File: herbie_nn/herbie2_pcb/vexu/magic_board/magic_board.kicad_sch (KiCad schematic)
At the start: 87 parts, among them J1 4P4C, J2 Conn_ARM_JTAG_SWD_10, J3 USB_C_Receptacle_USB2.0_14P, J4 Conn_01x04_Socket, J5 Conn_01x05_Pin, J6 Conn_01x05_Pin, J7 Conn_01x05_Pin, Q2 MMBT3904, U11 74LVC125, U12 AMS1117-5.0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

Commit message: added level shifters for led strips
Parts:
- added C14: 22uF, Capacitor_SMD:C_1206_3216Metric, symbol Device:C
- added U3, U9: 74LVC2T45DC, Package_SO:VSSOP-8_2.3x2mm_P0.5mm, symbol Logic_LevelTranslator:74LVC2T45DC
- C1, C2: value 15pF -> 12pF
- R4, R5, R6: value 330 -> 2K
- Y2: footprint Crystal:Crystal_SMD_2012-2Pin_2.0x1.2mm_HandSoldering -> Crystal:Crystal_SMD_5032-2Pin_5.0x3.2mm
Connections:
- net +12V: now also C14.1
- net +3.3V: now also U3.1 (VCCA), U3.5 (DIR), U9.1 (VCCA), U9.5 (DIR)
- net +5V: now also U3.8 (VCCB), U9.8 (VCCB)
- net GND: now also C14.2, U3.4 (GND), U9.4 (GND)
- net LED_SIG1: now also U3.2 (1A); no longer LEDSTRIP1.2 (Pin_2)
- net LED_SIG2: now also U9.2 (1A); no longer LEDSTRIP2.2 (Pin_2)
- net LED_SIG3: now also U3.3 (2A); no longer LEDSTRIP3.2 (Pin_2)
- new net LED_SIG1_OUT: LEDSTRIP1.2 (Pin_2), U3.7 (1B)
- new net LED_SIG2_OUT: LEDSTRIP2.2 (Pin_2), U9.7 (1B)
- new net LED_SIG3_OUT: LEDSTRIP3.2 (Pin_2), U3.6 (2B)
- no-connect marks 33 -> 35
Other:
- moved on the sheet: ENC1, ENC2, ENC3, ENC4, JP1, JP2, JP3, JP4, LED1, LED2, LEDSTRIP1, LEDSTRIP2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

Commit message: updated board
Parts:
- removed JP_D+1, JP_D-1, JP_RX1, JP_TX1: Jumper, Jumper:SolderJumper-2_P1.3mm_Open_Pad1.0x1.5mm, symbol Jumper:SolderJumper_2_Bridged
- added F2: 1A, Fuse:Fuse_1206_3216Metric, symbol Device:Fuse
- added PWR2: Jumper, Jumper:SolderJumper-2_P1.3mm_Open_Pad1.0x1.5mm, symbol Jumper:SolderJumper_2_Bridged
- added TP1, TP2: TestPoint, TestPoint:TestPoint_Pad_1.0x1.0mm, symbol Connector:TestPoint
- R13: value R -> 0K
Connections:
- net +12V: now also PWR2.2 (B); no longer J1.4, LEDSTRIP1.3 (Pin_3), LEDSTRIP2.3 (Pin_3), LEDSTRIP3.3 (Pin_3)
- net +3.3V: now also J4.3 (Pin_3); no longer J4.1 (Pin_1)
- net +5V: now also LEDSTRIP1.1 (Pin_1), LEDSTRIP2.1 (Pin_1), LEDSTRIP3.1 (Pin_1), F2.1; no longer D3.1 (K)
- net GND: now also LEDSTRIP1.3 (Pin_3), LEDSTRIP2.3 (Pin_3), LEDSTRIP3.3 (Pin_3); no longer LEDSTRIP1.1 (Pin_1), LEDSTRIP2.1 (Pin_1), LEDSTRIP3.1 (Pin_1)
- net RX_BRAIN: now also U4.59 (PB30)
- net SCL: now also J4.1 (Pin_1); no longer J4.2 (Pin_2)
- net SDA: now also J4.2 (Pin_2); no longer J4.3 (Pin_3)
- net TX_BRAIN: now also U4.60 (PB31)
- net at R2.1: now also U1.7 (B)
- net at U1.6 (A): now also R1.1
- net at U4.39 (PB16): now also TP1.1
- net at U4.40 (PB17): now also TP2.1
- new net: D3.1 (K), F2.2
- new net: J1.4, PWR2.1 (A)
- no-connect marks 35 -> 33

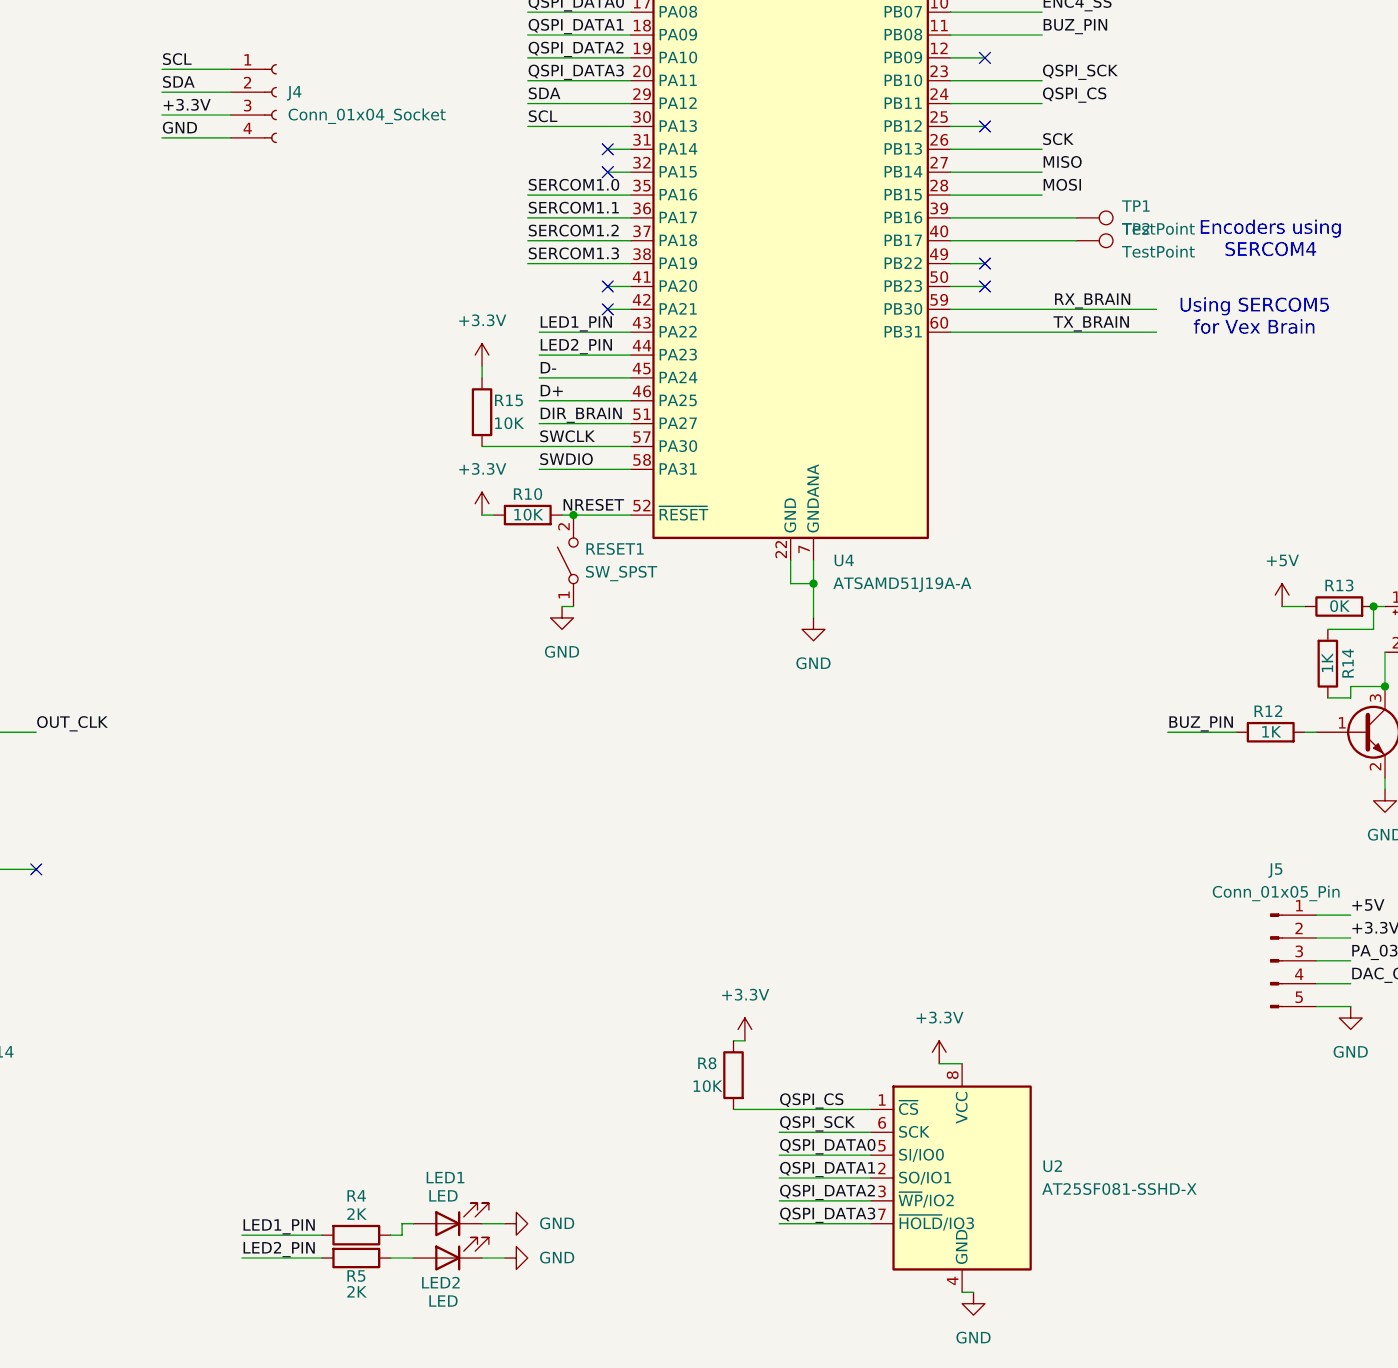
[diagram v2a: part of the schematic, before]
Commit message: removed qspi flash
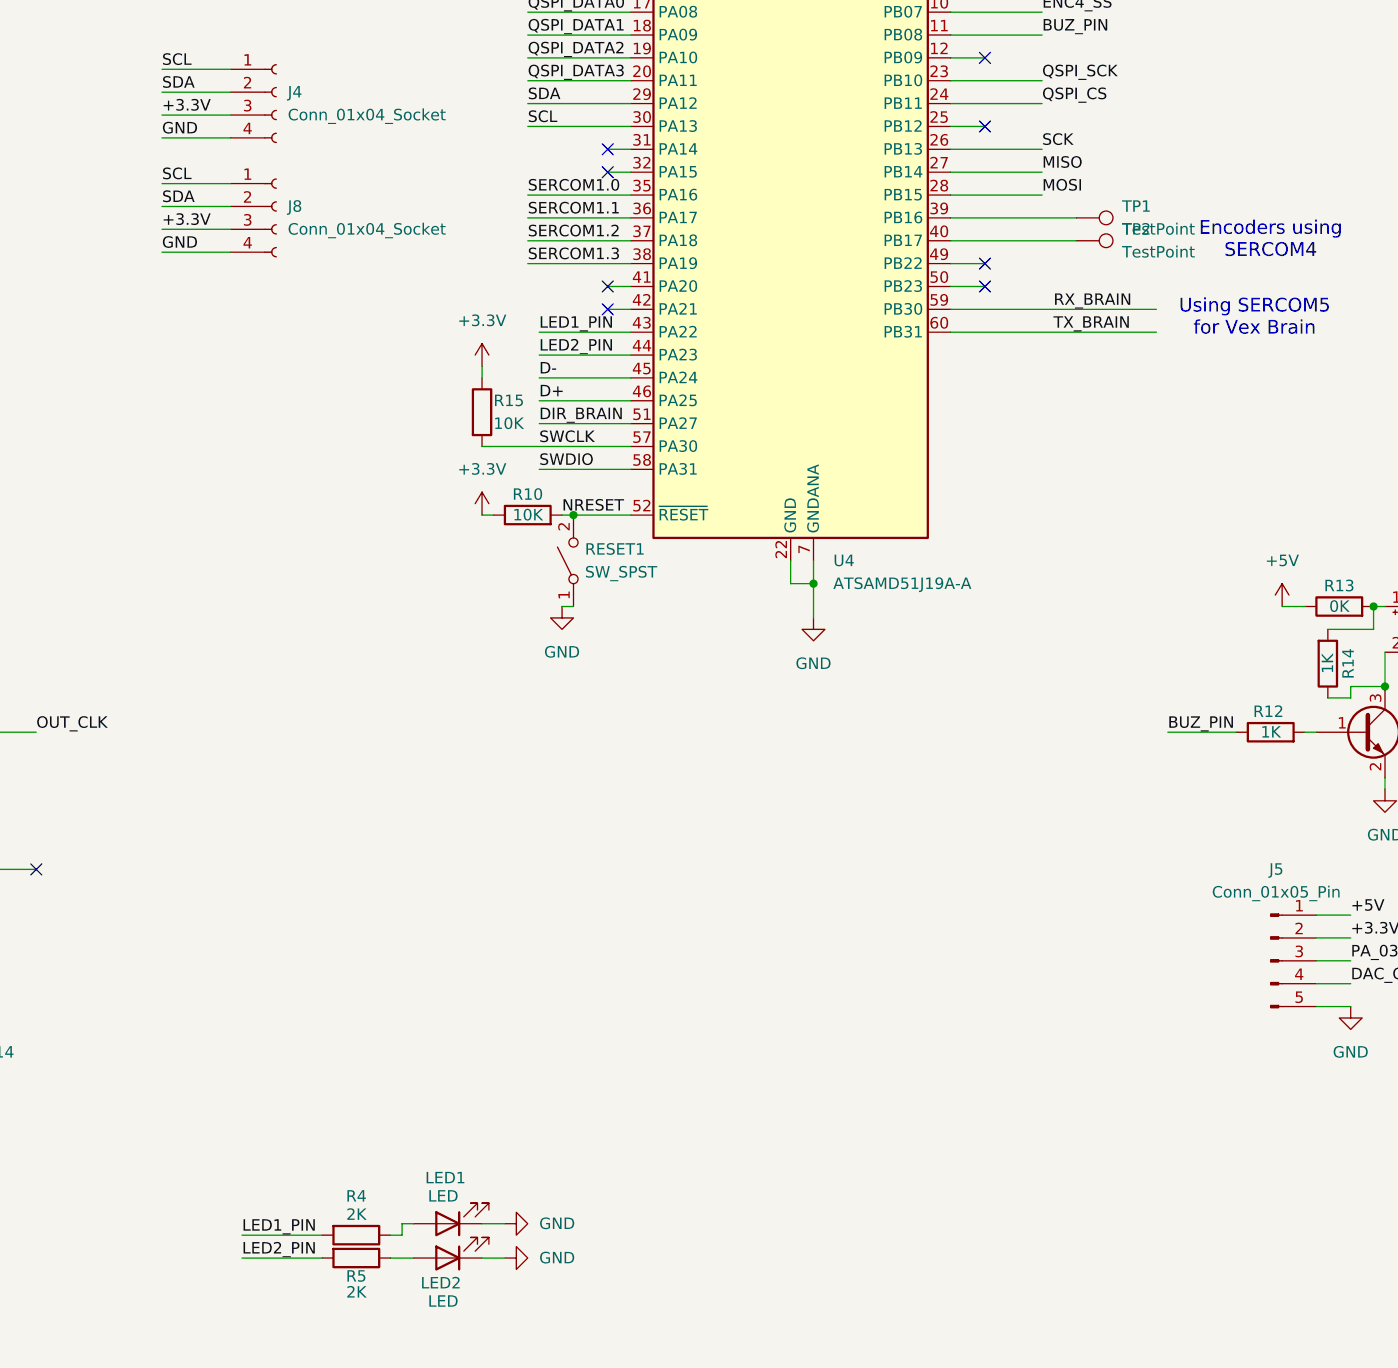
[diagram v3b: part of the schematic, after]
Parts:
- removed R8: 10K, Resistor_SMD:R_1206_3216Metric, symbol Device:R
- removed U2: AT25SF081-SSHD-X, Package_SO:SOIC-8_3.9x4.9mm_P1.27mm, symbol Memory_Flash:AT25SF081-SSHD-X
- added J8: Conn_01x04_Socket, Connector_JST:JST_SH_BM04B-SRSS-TB_1x04-1MP_P1.00mm_Vertical, symbol Connector:Conn_01x04_Socket
- J4: footprint Connector_PinHeader_1.27mm:PinHeader_1x04_P1.27mm_Vertical -> Connector_JST:JST_SH_BM04B-SRSS-TB_1x04-1MP_P1.00mm_Vertical
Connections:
- net +3.3V: now also J8.3 (Pin_3)
- net GND: now also J8.4 (Pin_4)
- net SCL: now also J8.1 (Pin_1)
- net SDA: now also J8.2 (Pin_2)

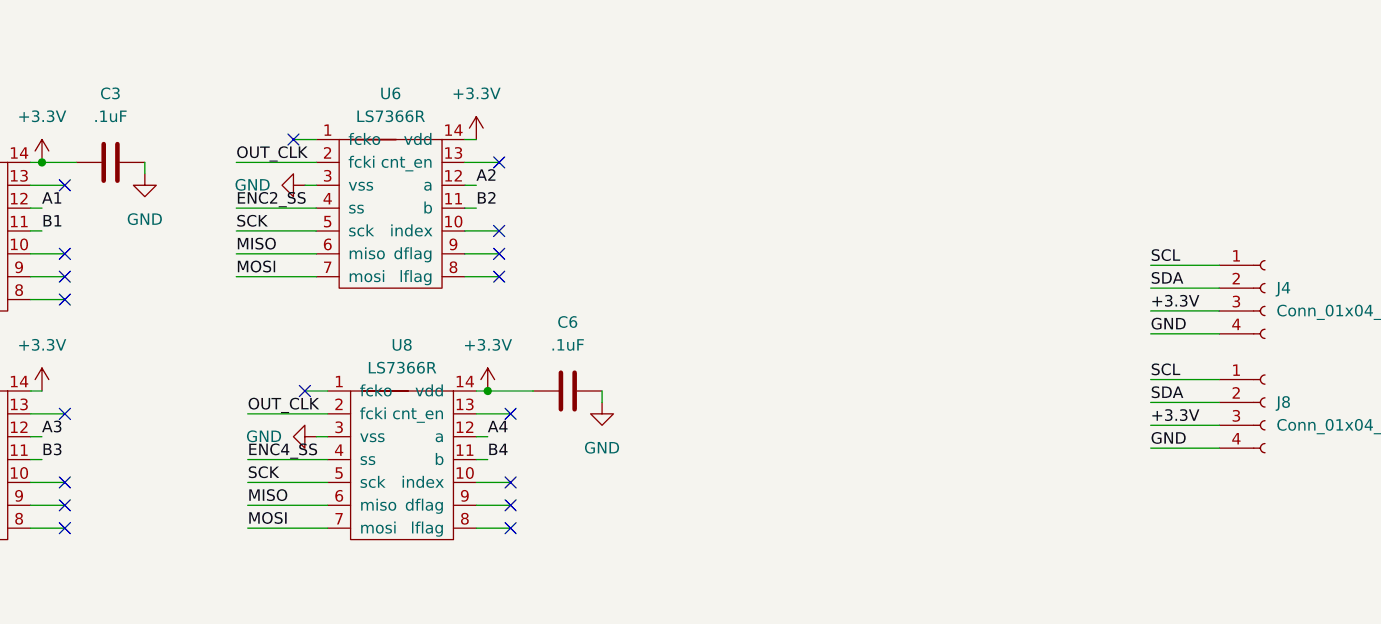
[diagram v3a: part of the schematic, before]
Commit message: added qwiic connectors
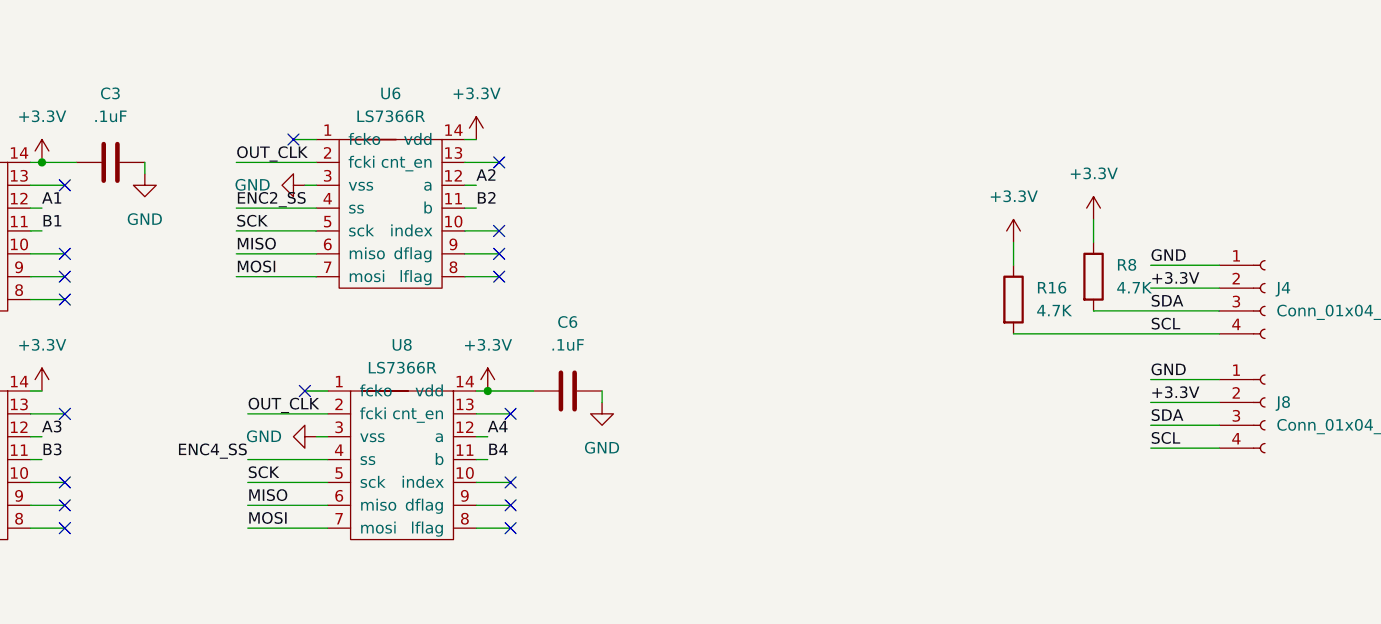
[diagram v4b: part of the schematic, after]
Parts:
- added R16, R8: 4.7K, Resistor_SMD:R_1206_3216Metric, symbol Device:R
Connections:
- net +3.3V: now also J4.2 (Pin_2), J8.2 (Pin_2), R16.1, R8.1; no longer J4.3 (Pin_3), J8.3 (Pin_3)
- net GND: now also J4.1 (Pin_1), J8.1 (Pin_1); no longer J4.4 (Pin_4), J8.4 (Pin_4)
- net SCL: now also J4.4 (Pin_4), J8.4 (Pin_4), R16.2; no longer J4.1 (Pin_1), J8.1 (Pin_1)
- net SDA: now also J4.3 (Pin_3), J8.3 (Pin_3), R8.2; no longer J4.2 (Pin_2), J8.2 (Pin_2)

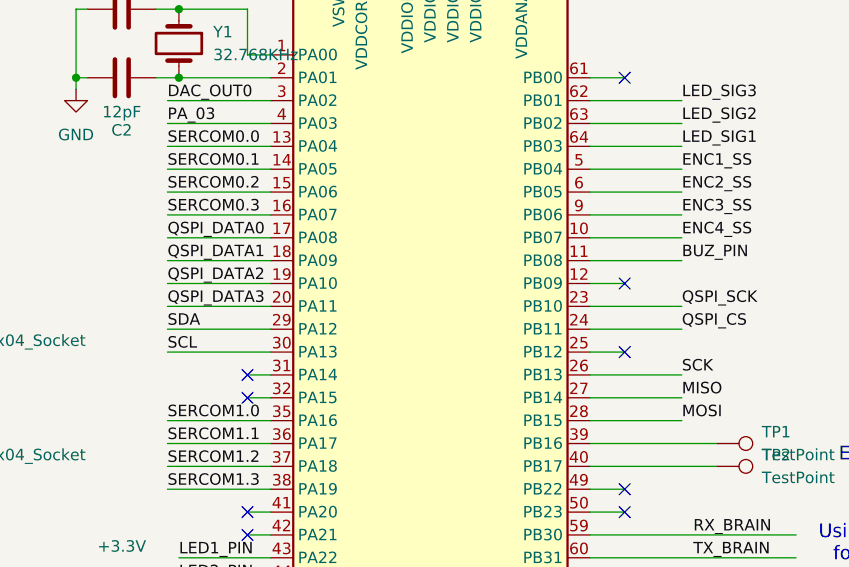
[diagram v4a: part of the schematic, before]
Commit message: fixed ground disconnect
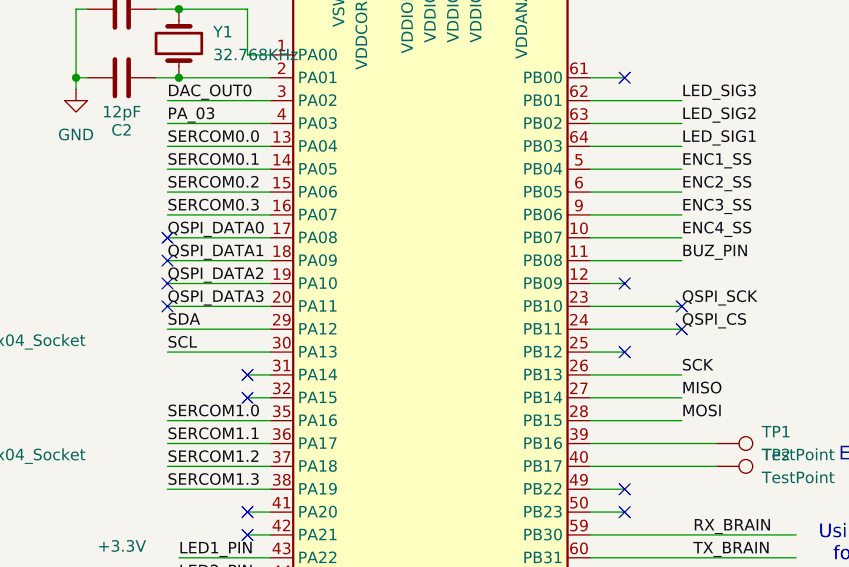
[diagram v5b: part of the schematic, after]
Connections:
- no-connect marks 33 -> 39
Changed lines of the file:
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@@
+	)
+	(no_connect
+		(at 217.17 134.62)
+	)
+	(no_connect
+		(at 217.17 139.7)
 	)
 	(no_connect
 		(at 353.06 191.77)
+	)
+	(no_connect
+		(at 217.17 137.16)
 	)
 	(no_connect
@@
 	)
 	(no_connect
+		(at 274.32 144.78)
+	)
+	(no_connect
 		(at 55.88 167.64)
 	)
@@
 	(no_connect
 		(at 33.02 154.94)
+	)
+	(no_connect
+		(at 217.17 142.24)
 	)
 	(no_connect
@@
 	)
 	(no_connect
+		(at 274.32 142.24)
+	)
+	(no_connect
